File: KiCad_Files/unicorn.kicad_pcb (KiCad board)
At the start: 2 copper layers, 68.8 x 71.1 mm, 11 parts, among them SW1 SW_DIP_x01

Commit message: pendand 0.1 experiments
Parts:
- removed D4: LED, Binary_Kitchen:5mm_SMD-Pad
- removed the REF** at (196.8, 60.2)
- removed Ref**: Val**, Binary_Kitchen:unicorn01
- removed ce_icon_mask_cu_3mm: G***, blinkyparts:ce-icon_Mask_Cu_3mm
- removed rohs_icon_mask_cu_3mm: G***, blinkyparts:rohs-icon_Mask_Cu_3mm
- removed weee_icon_mask_cu_3mm: G***, blinkyparts:weee-icon_Mask_Cu_3mm
- added G***: LOGO, LOGO, B.Cu at (91.0, 84.5)
- added G***: LOGO, LOGO, B.Cu at (131.5, 84.5)
- added REF**: Circular_Outline, Library:Circular_Outline, F.Cu at (111.0, 93.0)
- BT1: footprint Binary_Kitchen:BatteryHolder_Keystone_1060_1x2032_HandSoldering -> Battery:BatteryHolder_Keystone_1060_1x2032
- D1, D2, D3: footprint Binary_Kitchen:5mm_SMD-Pad -> LED_THT:LED_D5.0mm_Clear
- moved D2 122.6 mm to (88.0, 92.5)
- moved D3 101.8 mm to (111.0, 115.0), turned to 90 degrees
- moved BT1 84.4 mm to (111.0, 97.0)
- moved SW1 77.4 mm to (123.0, 80.0), turned to 180 degrees
- moved D1 44.9 mm to (134.0, 92.5), turned to 180 degrees
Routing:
- net VCC: track 78.9 -> 10.0 mm, vias 0 -> 4
- net +3V0: track 51.9 -> 18.5 mm
- net GND: track 112.5 -> 79.1 mm, vias 0 -> 4
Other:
- board size 68.8 x 71.1 mm -> 50 x 49.9 mm
- board text added: "+"
- board text added: "-"
- board text added: "Decorate front side"
- board text added: "LED's long leg = +"
- board text added: "battery holder battery's (+) towards you rights arms over battery > < left arms below battery"
- board text added: "button (bend legs)"
- board text removed: "CC-BY-SA 4.0"
- board text removed: "Design by: blinkyparts GmbH Egerstr. 9 93057 Regensburg"
- board text removed: "Unicorn"
- board text removed: "v1.2"

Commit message: v0.2 adding board to repo, adding gnd flood fill and a new transparent window
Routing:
- added copper zone on B.Cu, net GND
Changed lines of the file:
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@@
 		(fp_poly
 			(pts
-				(xy 0.011 -14.776) (xy 0.063 -14.67) (xy 0.164 -14.453) (xy 0.299 -14.16) (xy 0.451 -13.828) (xy 0.605 -13.491)
-				(xy 0.744 -13.184) (xy 0.764 -13.14) (xy 1.654 -11.121) (xy 2.488 -9.152) (xy 3.261 -7.244) (xy 3.968 -5.409)
-				(xy 4.607 -3.657) (xy 5.172 -2.002) (xy 5.659 -0.452) (xy 6.064 0.979) (xy 6.196 1.49) (xy 6.487 2.758)
-				(xy 6.698 3.907) (xy 6.826 4.934) (xy 6.872 5.834) (xy 6.838 6.58) (xy 6.651 7.594) (xy 6.318 8.559)
-				(xy 5.849 9.459) (xy 5.253 10.28) (xy 4.541 11.008) (xy 3.723 11.63) (xy 3.055 12.012) (xy 2.119 12.397)
-				(xy 1.119 12.64) (xy 0.84 12.682) (xy 0.521 12.711) (xy 0.135 12.728) (xy -0.244 12.732) (xy -0.543 12.721)
-				(xy -0.56 12.719) (xy -1.618 12.547) (xy -2.6 12.236) (xy -3.515 11.784) (xy -3.846 11.576) (xy -4.664 10.933)
-				(xy -5.369 10.185) (xy -5.952 9.345) (xy -6.404 8.427) (xy -6.717 7.447) (xy -6.879 6.459) (xy -6.894 6.184)
-				(xy -6.9 5.823) (xy -6.898 5.446) (xy -6.887 5.127) (xy -6.881 5.03) (xy -6.746 3.938) (xy -6.525 2.728)
-				(xy -6.217 1.398) (xy -5.821 -0.054) (xy -5.335 -1.632) (xy -4.761 -3.338) (xy -4.224 -4.83) (xy -3.63 -6.397)
-				(xy -2.97 -8.056) (xy -2.264 -9.766) (xy -1.53 -11.483) (xy -0.786 -13.162) (xy -0.111 -14.63) (xy -0.042 -14.772)
-				(xy -0.01 -14.806)
-			)
-			(stroke
-				(width 0)
-				(type solid)
-			)
-			(fill yes)
-			(layer "F.SilkS")
-		)
-		(fp_poly
-			(pts
 				(xy 1.873 -26) (xy 2.562 -25.939) (xy 3.245 -25.859) (xy 3.923 -25.761) (xy 4.595 -25.645) (xy 5.26 -25.512)
 				(xy 5.919 -25.361) (xy 6.571 -25.192) (xy 7.216 -25.007) (xy 7.854 -24.804) (xy 8.485 -24.585) (xy 9.108 -24.35)
@@
 			(layers "B.Cu" "B.Mask" "B.Paste")
 			(net 3 "VCC")
+			(zone_connect 2)
 			(thermal_bridge_angle 90)
 			(options
@@
 			(layers "B.Cu" "B.Mask" "B.Paste")
 			(net 2 "GND")
+			(zone_connect 2)
 			(thermal_bridge_angle 90)
 			(options
@@
 		(net 3)
 	)
+	(zone
+		(net 0)
+		(net_name "")
+		(layers "*.Mask")
+		(hatch edge 0.5)
+		(connect_pads
+			(clearance 0.508)
+		)
+		(min_thickness 0.25)
+		(filled_areas_thickness no)
+		(fill yes
+			(thermal_gap 0.5)
+			(thermal_bridge_width 0.5)
+			(smoothing fillet)
+			(radius 1)
+		)
+		(polygon
+			(pts
+				(xy 123.444 105.664) (xy 123.444 107.696) (xy 113.792 111.76) (xy 104.14 111.252) (xy 96.012 105.664)
+			)
+		)
+	)
+	(zone
+		(net 0)
+		(net_name "")
+		(layer "B.Cu")
+		(hatch edge 0.5)
+		(connect_pads
+			(clearance 0)
+		)
+		(min_thickness 0.25)
+		(filled_areas_thickness no)
+		(keepout
+			(tracks allowed)
+			(vias allowed)
+			(pads allowed)
+			(copperpour not_allowed)
+			(footprints allowed)
+		)
+		(placement
+			(enabled no)
+			(sheetname "")
+		)
+		(fill
+			(thermal_gap 0.5)
+			(thermal_bridge_width 0.5)
+			(smoothing fillet)
+			(radius 1)
+		)
+		(polygon
+			(pts
+				(xy 125.476 105.664) (xy 113.792 112.268) (xy 104.14 110.744) (xy 96.52 105.664)
+			)
+		)
+	)
+	(zone
+		(net 0)
+		(net_name "")
+		(layer "B.Cu")
+		(hatch edge 0.5)
+		(connect_pads
+			(clearance 0)
+		)
+		(min_thickness 0.25)
+		(filled_areas_thickness no)
+		(keepout
+			(tracks allowed)
+			(vias allowed)
+			(pads allowed)
+			(copperpour not_allowed)
+			(footprints allowed)
+		)
+		(placement
+			(enabled no)
+			(sheetname "")
+		)
+		(fill
+			(thermal_gap 0.5)
+			(thermal_bridge_width 0.5)
+		)
+		(polygon
+			(pts
+				(xy 87.376 89.916) (xy 90.424 89.916) (xy 91.948 96.52) (xy 93.98 102.108) (xy 99.06 107.696) (xy 105.156 110.744)
+				(xy 116.332 111.76) (xy 123.952 107.696) (xy 128.016 102.108) (xy 130.048 97.536) (xy 131.064 90.932)
+				(xy 131.064 89.408) (xy 134.62 89.408) (xy 134.62 96.52) (xy 129.54 105.664) (xy 120.904 113.284)
+				(xy 112.776 115.824) (xy 102.616 113.792) (xy 94.488 108.712) (xy 88.9 99.568) (xy 86.868 91.948)
+			)
+		)
+	)
+	(zone
+		(net 0)
+		(net_name "")
+		(layer "B.Cu")
+		(hatch edge 0.5)
+		(connect_pads
+			(clearance 0)
+		)
+		(min_thickness 0.25)
+		(filled_areas_thickness no)
+		(keepout
+			(tracks allowed)
+			(vias allowed)
+			(pads allowed)
+			(copperpour not_allowed)
+			(footprints allowed)
+		)
+		(placement
+			(enabled no)
+			(sheetname "")
+		)
+		(fill
+			(thermal_gap 0.5)
+			(thermal_bridge_width 0.5)
+		)
+		(polygon
+			(pts
+				(xy 131.064 89.408) (xy 134.112 89.408) (xy 132.08 102.108) (xy 124.46 111.76) (xy 113.284 114.808)
+				(xy 104.648 115) (xy 97.536 109.728) (xy 90.424 102.108) (xy 87.376 95.504) (xy 88 89.408) (xy 90.424 89.408)
+				(xy 90.932 92.5) (xy 92.456 99.06) (xy 95.504 103.632) (xy 100.076 108.204) (xy 105.156 110.744)
+				(xy 115.316 111.76) (xy 126.492 105.664) (xy 130.048 97.536)
+			)
+		)
+	)
+	(zone
+		(net 2)
+		(net_name "GND")
+		(layer "B.Cu")
+		(hatch edge 0.5)
+		(connect_pads
+			(clearance 0.508)
+		)
+		(min_thickness 0.25)
+		(filled_areas_thickness no)
+		(fill yes
+			(thermal_gap 0.5)
+			(thermal_bridge_width 0.5)
+		)
+		(polygon
+			(pts
+				(xy 142.748 108.712) (xy 142.748 122.428) (xy 81.28 122.428) (xy 81.28 60.96) (xy 142.24 60.96)
+			)
+		)
+	)
 	(embedded_fonts no)

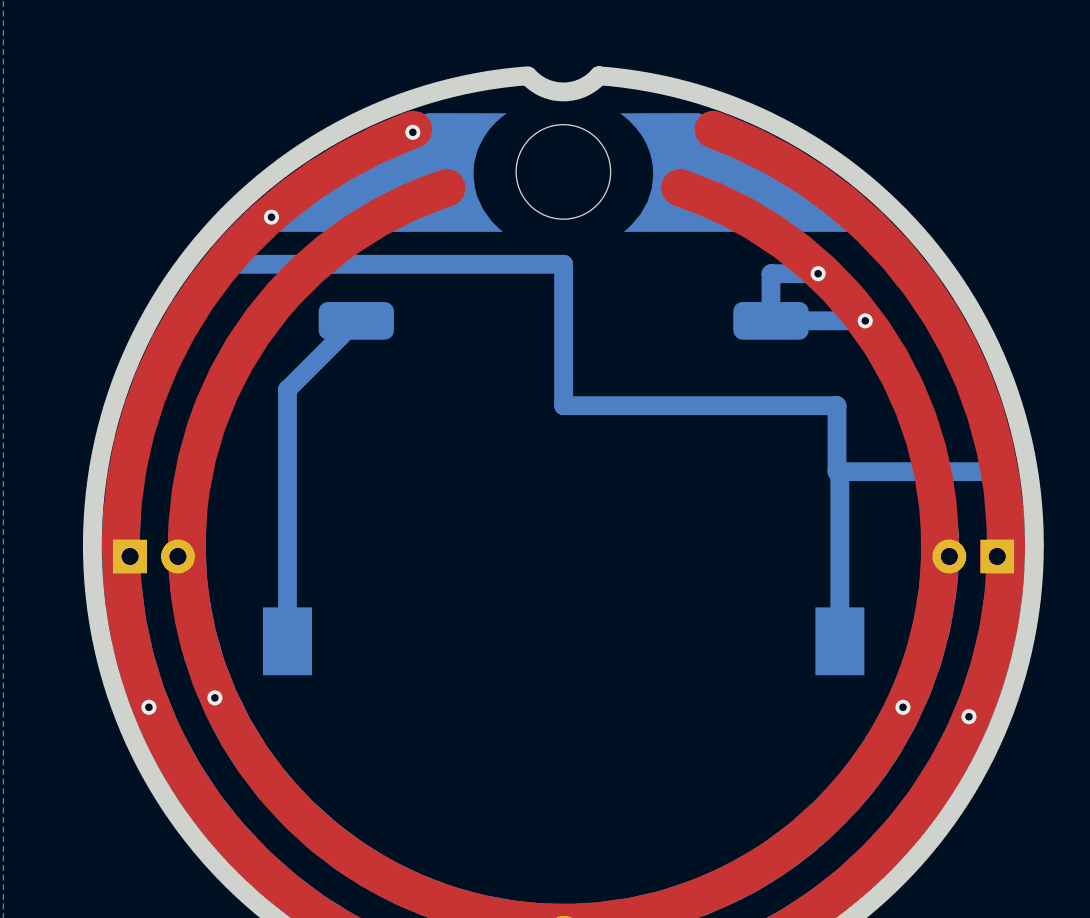
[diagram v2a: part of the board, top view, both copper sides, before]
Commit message: flood filling some vcc areas
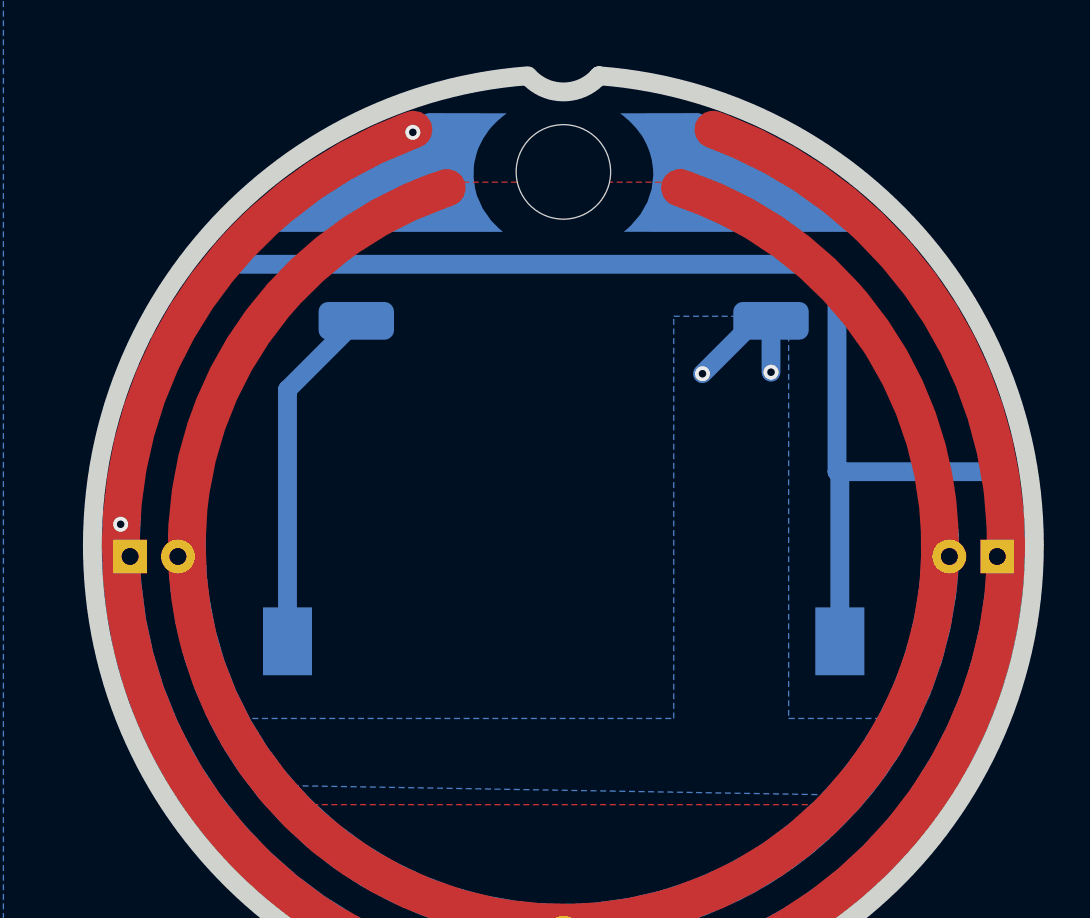
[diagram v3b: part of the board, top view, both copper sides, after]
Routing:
- net VCC: track 10.0 -> 7.52 mm, vias 4 -> 2
- net GND: track 79.1 -> 78.4 mm, vias 4 -> 2
- added copper zone on B.Cu, net VCC
- added copper zone on F.Cu, net VCC
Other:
- board text added: "- - - - - -"
- board text added: "area not connected"
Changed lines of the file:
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@@
 		(fp_poly
 			(pts
-				(xy -5.09 -24.015) (xy -3.013 -24.01) (xy -3.212 -23.861) (xy -3.483 -23.631) (xy -3.764 -23.354)
-				(xy -3.945 -23.148) (xy -4.248 -22.703) (xy -4.496 -22.223) (xy -4.55 -22.09) (xy -4.642 -21.793)
-				(xy -4.723 -21.449) (xy -4.761 -21.22) (xy -4.776 -20.63) (xy -4.699 -20.019) (xy -4.599 -19.639)
-				(xy -4.285 -18.941) (xy -3.842 -18.311) (xy -3.4 -17.872) (xy -3.219 -17.72) (xy -10.361 -17.72)
-				(xy -17.504 -17.72) (xy -17.384 -17.855) (xy -17.251 -17.995) (xy -17.039 -18.209) (xy -16.787 -18.459)
-				(xy -16.53 -18.709) (xy -16.306 -18.922) (xy -16.22 -19.002) (xy -15.013 -20.02) (xy -13.694 -20.977)
-				(xy -12.309 -21.841) (xy -12.012 -22.009) (xy -10.473 -22.786) (xy -8.861 -23.458) (xy -7.438 -23.939)
-				(xy -7.167 -24.02)
-			)
-			(stroke
-				(width 0)
-				(type solid)
-			)
-			(fill yes)
-			(layer "B.Cu")
-		)
-		(fp_poly
-			(pts
 				(xy 7.471 -23.92) (xy 9.116 -23.348) (xy 10.699 -22.668) (xy 10.79 -22.624) (xy 11.051 -22.496)
 				(xy 11.373 -22.331) (xy 11.701 -22.16) (xy 11.977 -22.013) (xy 12.098 -21.946) (xy 13.35 -21.184)
@@
 		(fp_poly
 			(pts
-				(xy -5.09 -24.015) (xy -3.013 -24.01) (xy -3.212 -23.861) (xy -3.483 -23.631) (xy -3.764 -23.354)
-				(xy -3.945 -23.148) (xy -4.248 -22.703) (xy -4.496 -22.223) (xy -4.55 -22.09) (xy -4.642 -21.793)
-				(xy -4.723 -21.449) (xy -4.761 -21.22) (xy -4.776 -20.63) (xy -4.699 -20.019) (xy -4.599 -19.639)
-				(xy -4.285 -18.941) (xy -3.842 -18.311) (xy -3.4 -17.872) (xy -3.219 -17.72) (xy -10.361 -17.72)
-				(xy -17.504 -17.72) (xy -17.384 -17.855) (xy -17.251 -17.995) (xy -17.039 -18.209) (xy -16.787 -18.459)
-				(xy -16.53 -18.709) (xy -16.306 -18.922) (xy -16.22 -19.002) (xy -15.013 -20.02) (xy -13.694 -20.977)
-				(xy -12.309 -21.841) (xy -12.012 -22.009) (xy -10.473 -22.786) (xy -8.861 -23.458) (xy -7.438 -23.939)
-				(xy -7.167 -24.02)
-			)
-			(stroke
-				(width 0)
-				(type solid)
-			)
-			(fill yes)
-			(layer "B.Mask")
-		)
-		(fp_poly
-			(pts
 				(xy 7.471 -23.92) (xy 9.116 -23.348) (xy 10.699 -22.668) (xy 10.79 -22.624) (xy 11.051 -22.496)
 				(xy 11.373 -22.331) (xy 11.701 -22.16) (xy 11.977 -22.013) (xy 12.098 -21.946) (xy 13.35 -21.184)
@@
 			(layers "F.Cu" "F.Mask" "F.Paste")
 			(net 2 "GND")
+			(zone_connect 2)
 			(thermal_bridge_angle 90)
 			(options
@@
 			(layers "F.Cu" "F.Mask" "F.Paste")
 			(net 3 "VCC")
+			(zone_connect 2)
 			(thermal_bridge_angle 90)
 			(options
@@
 			)
 		)
+		(pad "7" smd custom
+			(at -5.5 -22.703)
+			(size 1.27 1.27)
+			(layers "B.Cu" "B.Mask" "B.Paste")
+			(net 2 "GND")
+			(zone_connect 2)
+			(thermal_bridge_angle 90)
+			(options
+				(clearance outline)
+				(anchor circle)
+			)
+			(primitives
+				(gr_poly
+					(pts
+						(xy 0.41 -1.312) (xy 2.487 -1.307) (xy 2.288 -1.158) (xy 2.017 -0.928) (xy 1.736 -0.651) (xy 1.555 -0.445)
+						(xy 1.252 0) (xy 1.004 0.48) (xy 0.95 0.613) (xy 0.858 0.91) (xy 0.777 1.254) (xy 0.739 1.483)
+						(xy 0.724 2.073) (xy 0.801 2.684) (xy 0.901 3.064) (xy 1.215 3.762) (xy 1.658 4.392) (xy 2.1 4.831)
+						(xy 2.281 4.983) (xy -4.861 4.983) (xy -12.004 4.983) (xy -11.884 4.848) (xy -11.751 4.708) (xy -11.539 4.494)
+						(xy -11.287 4.244) (xy -11.03 3.994) (xy -10.806 3.781) (xy -10.72 3.701) (xy -9.513 2.683) (xy -8.194 1.726)
+						(xy -6.809 0.862) (xy -6.512 0.694) (xy -4.973 -0.083) (xy -3.361 -0.755) (xy -1.938 -1.236) (xy -1.667 -1.317)
+					)
+					(width 0)
+					(fill yes)
+				)
+			)
+		)
 		(embedded_fonts no)
 	)
@@
 		)
 	)
-	(gr_text "-"
+	(gr_text "- - - - - - "
 		(at 106.5 76.5 0)
 		(layer "B.SilkS")
@@
 		)
 	)
+	(gr_text "area not connected"
+		(at 129.032 76.708 0)
+		(layer "B.SilkS")
+		(effects
+			(font
+				(size 1 1)
+				(thickness 0.15)
+			)
+			(justify left bottom mirror)
+		)
+	)
 	(gr_text "+"
-		(at 122.5 82.5 0)
+		(at 120.396 82.804 0)
 		(layer "B.SilkS")
 		(effects
@@
 	)
 	(gr_text "LED's long leg = +"
-		(at 118 109 0)
+		(at 118 104.648 0)
 		(layer "B.SilkS")
 		(effects
@@
 	)
 	(via
-		(at 132.5 101)
-		(size 0.8)
-		(drill 0.4)
-		(layers "F.Cu" "B.Cu")
-		(net 2)
-	)
-	(via
-		(at 89 100.5)
-		(size 0.8)
-		(drill 0.4)
-		(layers "F.Cu" "B.Cu")
-		(net 2)
-	)
-	(via
 		(at 103 70)
 		(size 0.8)
@@
 	)
 	(via
-		(at 95.5 74.5)
+		(at 87.5 90.79)
 		(size 0.8)
 		(drill 0.4)
@@
 	)
 	(segment
-		(start 88 88.548009)
-		(end 87.5 89.048009)
+		(start 125.5 88)
+		(end 125.5 78.256)
 		(width 1)
 		(layer "B.Cu")
@@
 	)
 	(segment
-		(start 125.5 84.5)
-		(end 111 84.5)
+		(start 91 80)
+		(end 90 81)
 		(width 1)
 		(layer "B.Cu")
@@
 	)
 	(segment
-		(start 89 84.5)
-		(end 88.5 85)
+		(start 124.244 77)
+		(end 93 77)
 		(width 1)
 		(layer "B.Cu")
@@
 	)
 	(segment
-		(start 89.5 83)
-		(end 89 83.5)
-		(width 1)
-		(layer "B.Cu")
-		(net 2)
-	)
-	(segment
-		(start 93 77)
-		(end 91 79)
+		(start 89.5 82)
+		(end 89.5 83)
 		(width 1)
 		(layer "B.Cu")
@@
 	)
 	(segment
-		(start 91 80)
-		(end 90 81)
+		(start 125.5 78.256)
+		(end 124.244 77)
 		(width 1)
 		(layer "B.Cu")
@@
 	)
 	(segment
-		(start 87.5 89.048009)
-		(end 87.5 90.79)
+		(start 90 81.5)
+		(end 89.5 82)
 		(width 1)
 		(layer "B.Cu")
@@
 	)
 	(segment
-		(start 89 83.5)
-		(end 89 84.5)
+		(start 88.5 86)
+		(end 88 86.5)
 		(width 1)
 		(layer "B.Cu")
@@
 	)
 	(segment
-		(start 111 77)
-		(end 93 77)
+		(start 88 86.5)
+		(end 88 88.548009)
 		(width 1)
 		(layer "B.Cu")
@@
 	)
 	(segment
-		(start 111 84.5)
-		(end 111 77)
+		(start 93 77)
+		(end 91 79)
 		(width 1)
 		(layer "B.Cu")
@@
 	)
 	(segment
-		(start 90 81)
-		(end 90 81.5)
+		(start 89 83.5)
+		(end 89 84.5)
 		(width 1)
 		(layer "B.Cu")
@@
 	)
 	(segment
-		(start 88.5 86)
-		(end 88 86.5)
+		(start 89.5 83)
+		(end 89 83.5)
 		(width 1)
 		(layer "B.Cu")
@@
 	)
 	(segment
-		(start 88.5 85)
-		(end 88.5 86)
+		(start 87.5 89.048009)
+		(end 87.5 90.79)
 		(width 1)
 		(layer "B.Cu")
@@
 	)
 	(segment
-		(start 125.5 88)
-		(end 125.5 84.5)
+		(start 89 84.5)
+		(end 88.5 85)
 		(width 1)
 		(layer "B.Cu")
@@
 	)
 	(segment
-		(start 88 86.5)
-		(end 88 88.548009)
+		(start 88.5 85)
+		(end 88.5 86)
 		(width 1)
 		(layer "B.Cu")
@@
 	)
 	(segment
-		(start 89.5 82)
-		(end 89.5 83)
+		(start 91 79)
+		(end 91 80)
 		(width 1)
 		(layer "B.Cu")
@@
 	)
 	(segment
-		(start 91 79)
-		(end 91 80)
+		(start 88 88.548009)
+		(end 87.5 89.048009)
 		(width 1)
 		(layer "B.Cu")
@@
 	)
 	(segment
-		(start 90 81.5)
-		(end 89.5 82)
+		(start 90 81)
+		(end 90 81.5)
 		(width 1)
 		(layer "B.Cu")
@@
 	)
 	(via
-		(at 92.5 100)
+		(at 118.364 82.804)
 		(size 0.8)
 		(drill 0.4)
@@
 	)
 	(via
-		(at 124.5 77.5)
-		(size 0.8)
-		(drill 0.4)
-		(layers "F.Cu" "B.Cu")
-		(net 3)
-	)
-	(via
-		(at 127 80)
-		(size 0.8)
-		(drill 0.4)
-		(layers "F.Cu" "B.Cu")
-		(net 3)
-	)
-	(via
-		(at 129 100.5)
+		(at 122 82.724)
 		(size 0.8)
 		(drill 0.4)
@@
 	)
 	(segment
-		(start 122 80)
-		(end 122 77.5)
+		(start 121.168 80)
+		(end 122 80)
 		(width 1)
 		(layer "B.Cu")
@@
 	)
 	(segment
-		(start 122 77.5)
-		(end 124.5 77.5)
+		(start 122 82.724)
+		(end 122 80)
 		(width 1)
 		(layer "B.Cu")
@@
 	)
 	(segment
-		(start 122 80)
-		(end 127 80)
+		(start 118.364 82.804)
+		(end 121.168 80)
 		(width 1)
 		(layer "B.Cu")
@@
 	)
 	(zone
+		(net 3)
+		(net_name "VCC")
+		(layer "F.Cu")
+		(hatch edge 0.5)
+		(priority 1)
+		(connect_pads
+			(clearance 0.508)
+		)
+		(min_thickness 0.25)
+		(filled_areas_thickness no)
+		(fill yes
+			(thermal_gap 0.5)
+			(thermal_bridge_width 0.5)
+			(smoothing fillet)
+			(radius 1)
+		)
+		(polygon
+			(pts
+				(xy 91.44 87.884) (xy 95.504 79.248) (xy 105.156 72.644) (xy 117.348 72.644) (xy 125.984 77.724)
+				(xy 131.064 89.408) (xy 129.54 98.552) (xy 125.476 105.664) (xy 96.52 105.664) (xy 91.44 96.52)
+			)
+		)
+	)
+	(zone
 		(net 0)
 		(net_name "")
@@
 			)
 		)
+	)
+	(zone
+		(net 3)
+		(net_name "VCC")
+		(layer "B.Cu")
+		(hatch edge 0.5)
+		(priority 2)
+		(connect_pads
+			(clearance 0.508)
+		)
+		(min_thickness 0.25)
+		(filled_areas_thickness no)
+		(fill yes
+			(thermal_gap 0.5)
+			(thermal_bridge_width 0.5)
+			(smoothing fillet)
+			(radius 1)
+		)
+		(polygon
+			(pts
+				(xy 128.016 102.108) (xy 125.984 105.156) (xy 96.012 104.648) (xy 92.964 101.092) (xy 116.84 101.092)
+				(xy 116.84 79.756) (xy 122.936 79.756) (xy 122.936 101.092) (xy 128.524 101.092)
+			)
+		)

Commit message: kicad 0.5
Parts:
- removed D1, D2, D3: LED, LED_THT:LED_D5.0mm_Clear
- removed the G*** at (91.0, 84.5)
- removed the REF** at (111.0, 93.0)
- added REF**: mushyrocket 0.5, blinkyparts:mushyrocket 0.5, F.Cu at (50.8, 151.9)
- added REF**: 5mm_SMD-Pad, blinkyparts:5mm_SMD-Pad, B.Cu at (33.3, 123.1)
- added REF**: 5mm_SMD-Pad, blinkyparts:5mm_SMD-Pad, B.Cu at (49.5, 122.1)
- added REF**: 5mm_SMD-Pad, blinkyparts:5mm_SMD-Pad, B.Cu at (67.3, 122.6)
- added REF**: 5mm_SMD-Pad, blinkyparts:5mm_SMD-Pad, B.Cu at (51.6, 174.9)
- moved SW1 122.7 mm to (39.8, 170.2), turned to 0 degrees
- moved G*** 110.5 mm to (74.7, 179.3)
- moved BT1 81.5 mm to (50.8, 151.9), turned to 180 degrees
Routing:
- net GND: track 78.4 -> 0.00 mm, vias 2 -> 0
- net VCC: track 7.52 -> 0.00 mm, vias 2 -> 0
- net +3V0: track 18.5 -> 20.4 mm
- removed copper zone on F.Cu, net VCC
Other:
- board size 50 x 49.9 mm -> 69.3 x 93.7 mm
- board text removed: "+"
- board text removed: "-"
- board text removed: "- - - - - -"
- board text removed: "area not connected"
